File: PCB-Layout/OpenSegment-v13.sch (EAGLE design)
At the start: 45 parts, among them Q1 PNP, Q10 MMBT2222, Q11 MMBT2222, Q12 MMBT2222, Q2 PNP, Q3 PNP, Q4 PNP, Q5 PNP, Q6 PNP, Q7 PNP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

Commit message: Added I2C gang pins, silk color squares, adjusted 10uF cap spot.
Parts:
- removed JP7: Serial, SparkFun-Connectors:M03
- removed SJ3: Counter Ctl, SparkFun-Passives:SOLDERJUMPERNO
- added C1: 0.1uF, SparkFun:CAP0402-CAP
- added JP11: Serial, SparkFun-Connectors:M03JST-PTH
- added JP12, JP13: (no value), SparkFun-Connectors:M02PTH
- added SJ1, SJ2: Counter Ctl, SparkFun-Passives:SOLDERJUMPERNO
- added U$4: OSHW-LOGOS, SparkFun-Aesthetics:OSHW-LOGOS
- JP8: value M01 -> RESET
- R2, R3, R4, R5, R6, R7, R8, R9: value 50 -> 27
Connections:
- net CS renamed !SS
- net MISO renamed SDO
- net MOSI renamed SDI
- removed net N$2: SJ3.1, U2.PB7(XTAL2/TOSC2)
- new net ANALOG: SJ2.1, U2.PB7(XTAL2/TOSC2)
- new net N$11: C1.2, U2.AREF
- net COUNTER: now also SJ1.1; no longer JP2.8
- net GND: now also C1.1, JP11.2, JP12.1, SJ1.2, SJ2.2; no longer JP7.2, SJ3.2
- net RAW: now also JP11.1, JP12.2; no longer JP7.3
- net RXI: now also JP11.3; no longer JP7.1
- net SCL: now also JP13.2
- net SDA: now also JP13.1
- net TXO: now also JP2.8
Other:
- note added: "50 Ohm"
- note added: "Add OSHW logo"
- note added: "Add silk to top side A6/7"
- note added: "Added mode jumpers"
- note added: "Changed SPI pins to SDO/SDI to match"
- note added: "Changes on v1.3:"
- note added: "Close Jumper For:"
- note added: "Decrement"
- note added: "Ganged I2C + pwr"
- note added: "Increment"
- note added: "Measurements show 10mA. Changing to 27 Ohm"
- note added: "Meter Mode"
- note added: "Move in 10uF cap"
- note added: "R = 38.3 Ohm"
- note added: "Silkscreen squares for colors"
- note added: "original S7S"
- note removed: "Changed PB6 to dedicated counter pin"
- note removed: "Removed TXO connection"
- moved on the sheet: C10, C13, C19, C3, C4, JP1, JP10, JP2, JP8, JP9, LED1, R1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

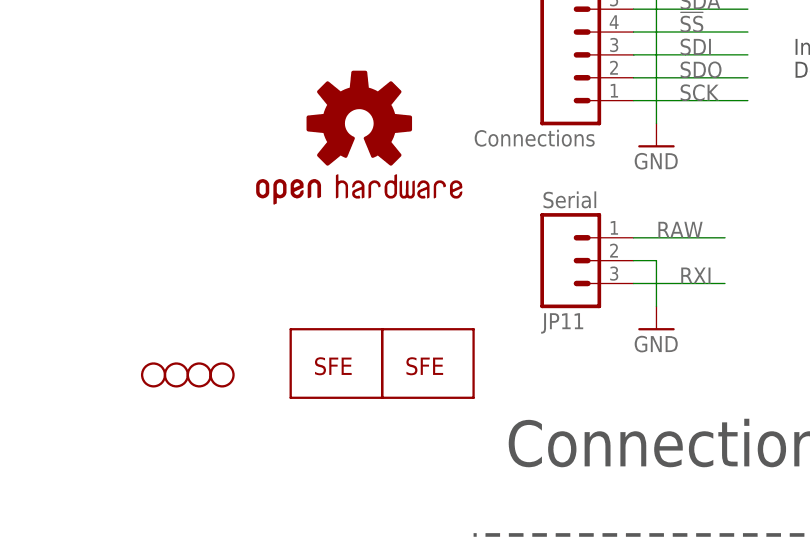
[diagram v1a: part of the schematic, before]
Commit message: Added fiducial markings and created panel
preparing for mass production
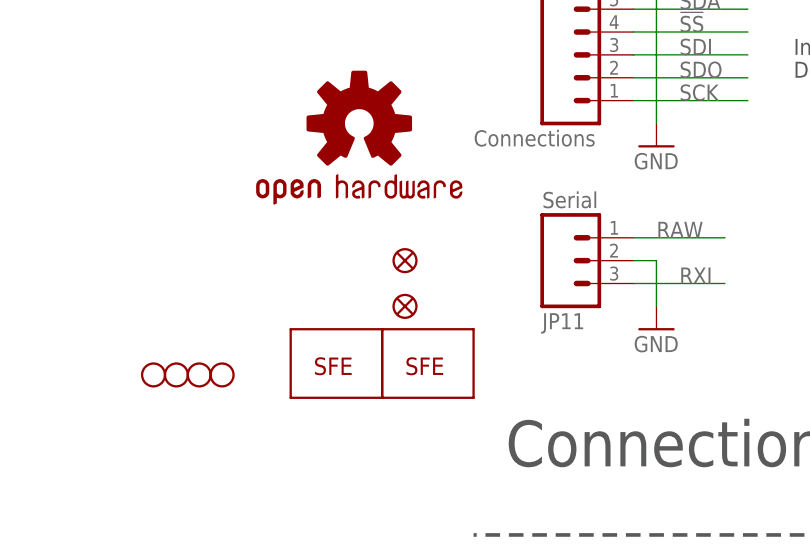
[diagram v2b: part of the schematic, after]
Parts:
- added JP14, JP7: FIDUCIALUFIDUCIAL, SparkFun:FIDUCIALUFIDUCIAL
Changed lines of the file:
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@@
 <part name="JP12" library="SparkFun-Connectors" deviceset="M02" device="PTH"/>
 <part name="JP13" library="SparkFun-Connectors" deviceset="M02" device="PTH"/>
+<part name="JP7" library="SparkFun" deviceset="FIDUCIAL" device="UFIDUCIAL"/>
+<part name="JP14" library="SparkFun" deviceset="FIDUCIAL" device="UFIDUCIAL"/>
 </parts>
 <sheets>
@@
 <instance part="JP12" gate="G$1" x="317.5" y="30.48"/>
 <instance part="JP13" gate="G$1" x="317.5" y="15.24"/>
+<instance part="JP7" gate="G$1" x="241.3" y="30.48"/>
+<instance part="JP14" gate="G$1" x="241.3" y="25.4"/>
 </instances>
 <busses>

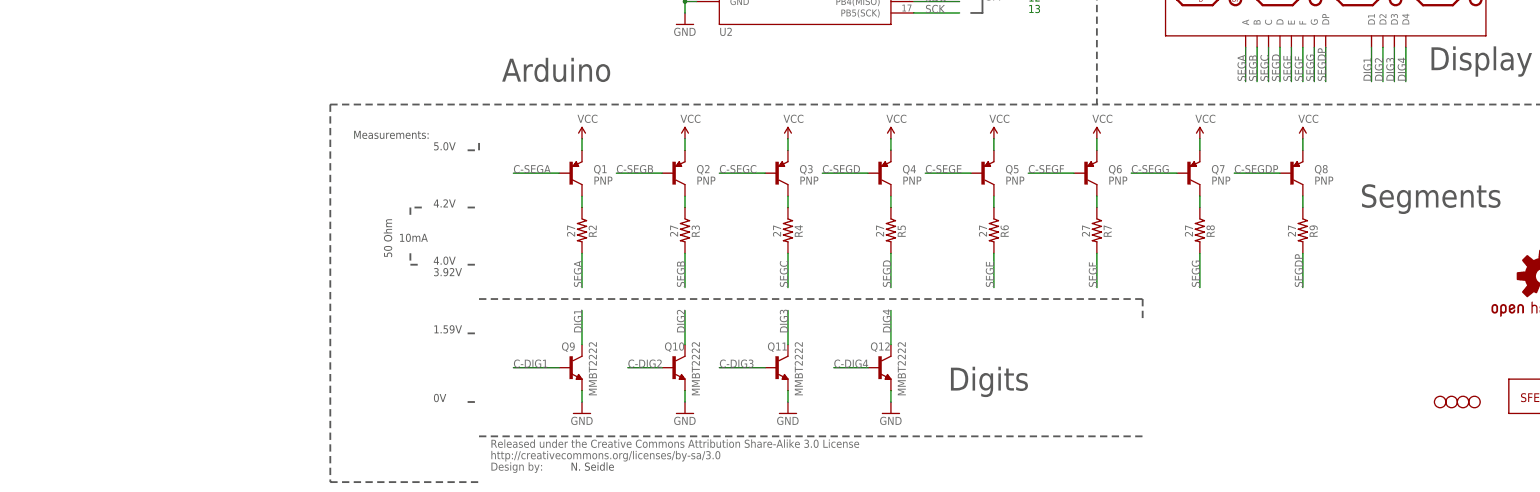
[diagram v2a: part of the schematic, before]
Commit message: Added part #s for transistors and resistor calculations.
The bias resistors on the NPN and PNPs helped. Reducing current through
segments further to hit 10-12mA per segment when on for 25% duty cycle.
Also added calculations for different color displays.
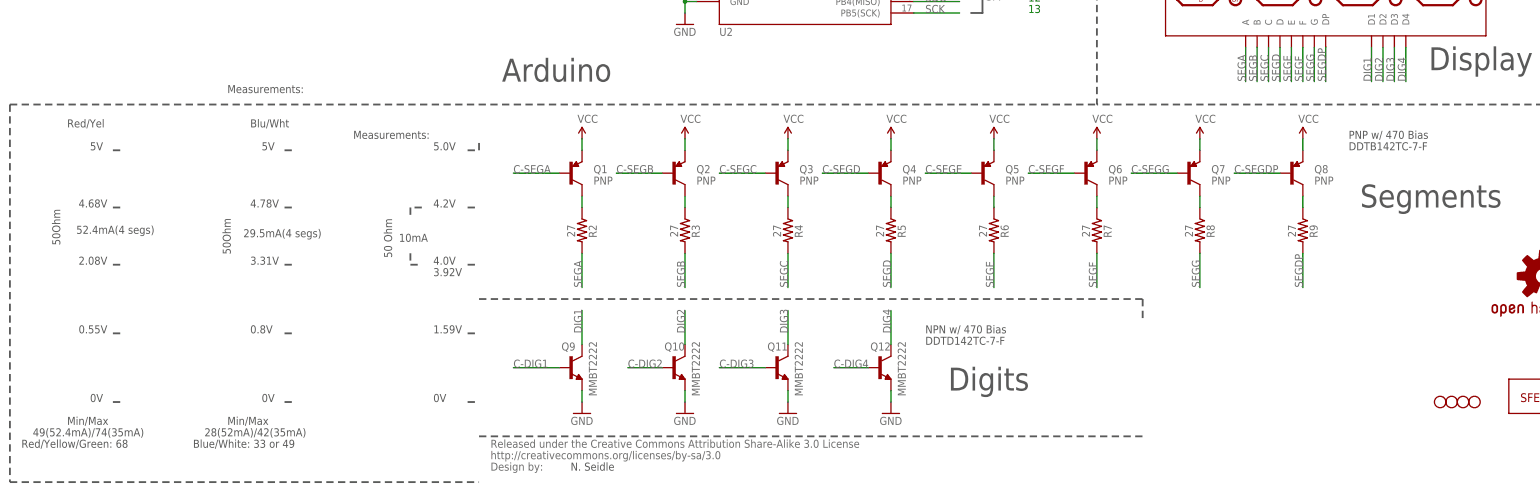
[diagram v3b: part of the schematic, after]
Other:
- note added: "0.55V"
- note added: "0.8V"
- note added: "2.08V"
- note added: "28(52mA)/42(35mA)"
- note added: "29.5mA(4 segs)"
- note added: "3.31V"
- note added: "4.68V"
- note added: "4.78V"
- note added: "49(52.4mA)/74(35mA)"
- note added: "50Ohm"
- note added: "52.4mA(4 segs)"
- note added: "5V"
- note added: "Blu/Wht"
- note added: "Blue/White: 33 or 49"
- note added: "DDTB142TC-7-F"
- note added: "DDTD142TC-7-F"
- note added: "Min/Max"
- note added: "NPN w/ 470 Bias"
- note added: "PNP w/ 470 Bias"
- note added: "Red/Yel"
- note added: "Red/Yellow/Green: 68"
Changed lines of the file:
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@@
 <text x="121.92" y="147.32" size="1.778" layer="91">A6</text>
 <text x="121.92" y="144.78" size="1.778" layer="91">A7</text>
-<wire x1="-33.02" y1="83.82" x2="137.16" y2="83.82" width="0.4064" layer="97" style="shortdash"/>
+<wire x1="-104.14" y1="83.82" x2="137.16" y2="83.82" width="0.4064" layer="97" style="shortdash"/>
 <wire x1="0" y1="40.64" x2="147.32" y2="40.64" width="0.4064" layer="97" style="shortdash"/>
 <wire x1="147.32" y1="40.64" x2="147.32" y2="35.56" width="0.4064" layer="97" style="shortdash"/>
@@
 <text x="284.48" y="50.8" size="1.778" layer="97">Decrement</text>
 <text x="185.42" y="167.64" size="1.778" layer="97">Added mode jumpers</text>
-<wire x1="-33.02" y1="83.82" x2="-33.02" y2="0" width="0.4064" layer="97" style="shortdash"/>
-<wire x1="-33.02" y1="0" x2="0" y2="0" width="0.4064" layer="97" style="shortdash"/>
+<wire x1="-104.14" y1="83.82" x2="-104.14" y2="0" width="0.4064" layer="97" style="shortdash"/>
+<wire x1="-104.14" y1="0" x2="0" y2="0" width="0.4064" layer="97" style="shortdash"/>
 <wire x1="-2.54" y1="60.96" x2="0" y2="60.96" width="0.4064" layer="97" style="shortdash"/>
 <wire x1="-2.54" y1="73.66" x2="0" y2="73.66" width="0.4064" layer="97" style="shortdash"/>
@@
 <text x="185.42" y="149.86" size="1.778" layer="97">Move in 10uF cap</text>
 <text x="182.88" y="154.94" size="1.778" layer="97">Changes on v1.3:</text>
+<text x="-55.88" y="86.36" size="1.778" layer="97">Measurements:</text>
+<text x="-50.8" y="60.96" size="1.778" layer="97">4.78V</text>
+<text x="-50.8" y="48.26" size="1.778" layer="97">3.31V</text>
+<text x="-50.8" y="33.02" size="1.778" layer="97">0.8V</text>
+<text x="-48.26" y="73.66" size="1.778" layer="97">5V</text>
+<text x="-48.26" y="17.78" size="1.778" layer="97">0V</text>
+<text x="-50.8" y="78.74" size="1.778" layer="97">Blu/Wht</text>
+<text x="-91.44" y="78.74" size="1.778" layer="97">Red/Yel</text>
+<text x="-86.36" y="73.66" size="1.778" layer="97">5V</text>
+<text x="-88.9" y="60.96" size="1.778" layer="97">4.68V</text>
+<text x="-88.9" y="48.26" size="1.778" layer="97">2.08V</text>
+<text x="-88.9" y="33.02" size="1.778" layer="97">0.55V</text>
+<text x="-86.36" y="17.78" size="1.778" layer="97">0V</text>
+<text x="-55.118" y="50.546" size="1.778" layer="97" rot="R90">50Ohm</text>
+<text x="-92.964" y="52.578" size="1.778" layer="97" rot="R90">50Ohm</text>
+<text x="-60.96" y="10.16" size="1.778" layer="97">28(52mA)/42(35mA)</text>
+<text x="-99.06" y="10.16" size="1.778" layer="97">49(52.4mA)/74(35mA)</text>
+<text x="-91.44" y="12.7" size="1.778" layer="97">Min/Max</text>
+<text x="-101.6" y="7.62" size="1.778" layer="97">Red/Yellow/Green: 68</text>
+<text x="-63.5" y="7.62" size="1.778" layer="97">Blue/White: 33 or 49</text>
+<text x="-55.88" y="12.7" size="1.778" layer="97">Min/Max</text>
+<wire x1="-43.18" y1="33.02" x2="-40.64" y2="33.02" width="0.4064" layer="97" style="shortdash"/>
+<wire x1="-81.28" y1="33.02" x2="-78.74" y2="33.02" width="0.4064" layer="97" style="shortdash"/>
+<wire x1="-43.18" y1="48.26" x2="-40.64" y2="48.26" width="0.4064" layer="97" style="shortdash"/>
+<wire x1="-43.18" y1="60.96" x2="-40.64" y2="60.96" width="0.4064" layer="97" style="shortdash"/>
+<wire x1="-43.18" y1="73.66" x2="-40.64" y2="73.66" width="0.4064" layer="97" style="shortdash"/>
+<wire x1="-43.18" y1="17.78" x2="-40.64" y2="17.78" width="0.4064" layer="97" style="shortdash"/>
+<wire x1="-81.28" y1="48.26" x2="-78.74" y2="48.26" width="0.4064" layer="97" style="shortdash"/>
+<wire x1="-81.28" y1="60.96" x2="-78.74" y2="60.96" width="0.4064" layer="97" style="shortdash"/>
+<wire x1="-81.28" y1="73.66" x2="-78.74" y2="73.66" width="0.4064" layer="97" style="shortdash"/>
+<wire x1="-81.28" y1="17.78" x2="-78.74" y2="17.78" width="0.4064" layer="97" style="shortdash"/>
+<text x="-89.408" y="55.118" size="1.778" layer="97">52.4mA(4 segs)</text>
+<text x="-52.324" y="54.356" size="1.778" layer="97">29.5mA(4 segs)</text>
+<text x="99.06" y="33.02" size="1.778" layer="97">NPN w/ 470 Bias</text>
+<text x="99.06" y="30.48" size="1.778" layer="97">DDTD142TC-7-F</text>
+<text x="193.04" y="76.2" size="1.778" layer="97">PNP w/ 470 Bias</text>
+<text x="193.04" y="73.66" size="1.778" layer="97">DDTB142TC-7-F</text>
 </plain>
 <instances>

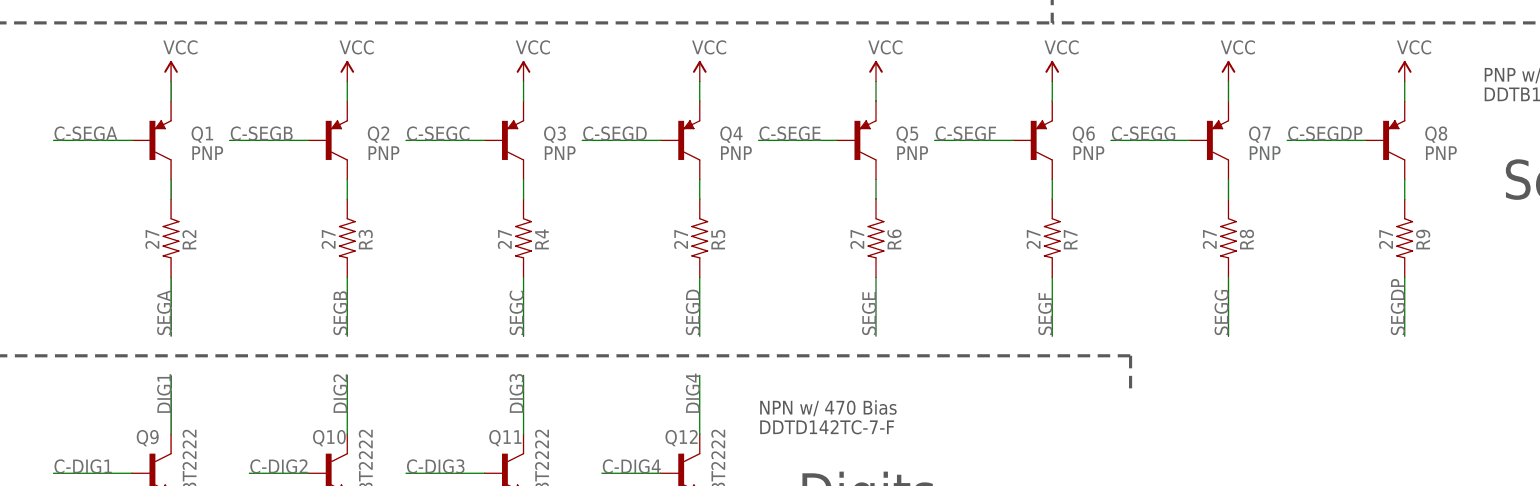
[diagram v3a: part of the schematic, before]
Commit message: Updated resistor values.
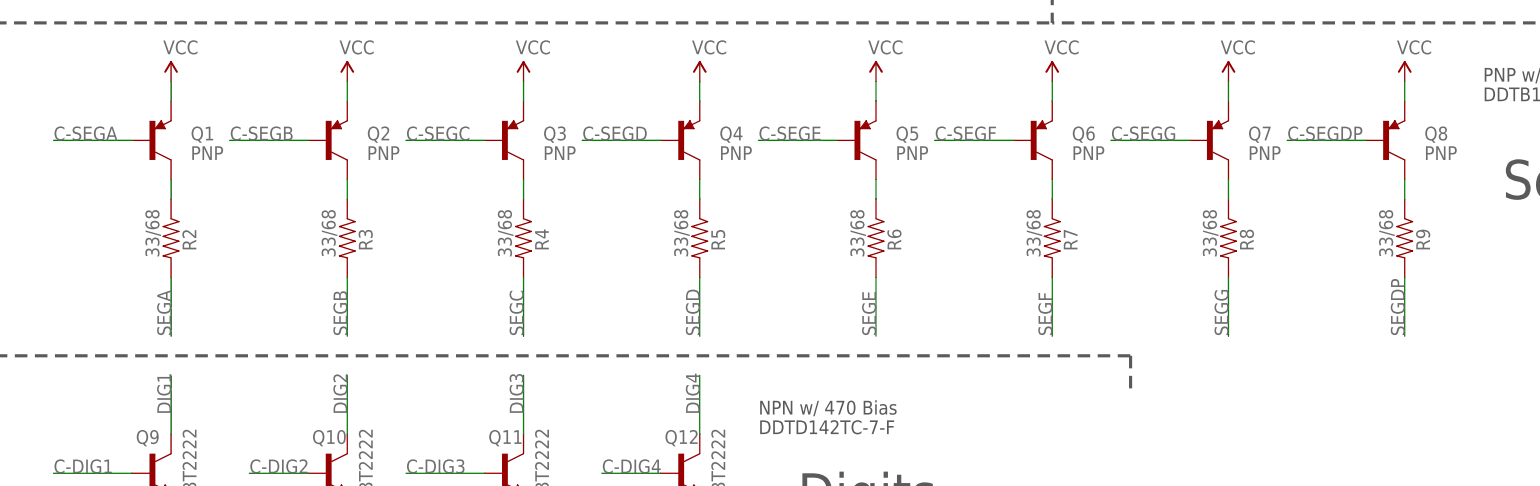
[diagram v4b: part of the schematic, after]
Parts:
- R2, R3, R4, R5, R6, R7, R8, R9: value 27 -> 33/68
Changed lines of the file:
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@@
 <part name="JP5" library="SparkFun-Electromechanical" deviceset="STAND-OFF" device=""/>
 <part name="JP6" library="SparkFun-Electromechanical" deviceset="STAND-OFF" device=""/>
-<part name="R2" library="SparkFun" deviceset="RESISTOR" device="0402-RES" value="27"/>
+<part name="R2" library="SparkFun" deviceset="RESISTOR" device="0402-RES" value="33/68"/>
 <part name="Q1" library="SparkFun-DiscreteSemi" deviceset="TRANSISTOR_PNP" device="SMD" value="PNP"/>
 <part name="SJ2" library="SparkFun-Passives" deviceset="SOLDERJUMPER" device="NO" value="Counter Ctl"/>
@@
 <part name="GND15" library="SparkFun" deviceset="GND" device=""/>
 <part name="JP2" library="SparkFun-Connectors" deviceset="M10" device="&quot;" value="Connections"/>
-<part name="R3" library="SparkFun" deviceset="RESISTOR" device="0402-RES" value="27"/>
-<part name="R4" library="SparkFun" deviceset="RESISTOR" device="0402-RES" value="27"/>
-<part name="R5" library="SparkFun" deviceset="RESISTOR" device="0402-RES" value="27"/>
-<part name="R6" library="SparkFun" deviceset="RESISTOR" device="0402-RES" value="27"/>
-<part name="R7" library="SparkFun" deviceset="RESISTOR" device="0402-RES" value="27"/>
-<part name="R8" library="SparkFun" deviceset="RESISTOR" device="0402-RES" value="27"/>
-<part name="R9" library="SparkFun" deviceset="RESISTOR" device="0402-RES" value="27"/>
+<part name="R3" library="SparkFun" deviceset="RESISTOR" device="0402-RES" value="33/68"/>
+<part name="R4" library="SparkFun" deviceset="RESISTOR" device="0402-RES" value="33/68"/>
+<part name="R5" library="SparkFun" deviceset="RESISTOR" device="0402-RES" value="33/68"/>
+<part name="R6" library="SparkFun" deviceset="RESISTOR" device="0402-RES" value="33/68"/>
+<part name="R7" library="SparkFun" deviceset="RESISTOR" device="0402-RES" value="33/68"/>
+<part name="R8" library="SparkFun" deviceset="RESISTOR" device="0402-RES" value="33/68"/>
+<part name="R9" library="SparkFun" deviceset="RESISTOR" device="0402-RES" value="33/68"/>
 <part name="GND16" library="SparkFun" deviceset="GND" device=""/>
 <part name="U$2" library="SparkFun" deviceset="LOGO-SFE" device="SK"/>
@@
 <instance part="R2" gate="G$1" x="22.86" y="55.88" smashed="yes" rot="R270">
 <attribute name="NAME" x="24.3586" y="57.15" size="1.778" layer="95" rot="R270"/>
-<attribute name="VALUE" x="19.558" y="57.15" size="1.778" layer="96" rot="R270"/>
+<attribute name="VALUE" x="19.558" y="59.69" size="1.778" layer="96" rot="R270"/>
 </instance>
 <instance part="Q1" gate="G$1" x="20.32" y="68.58"/>
@@
 <instance part="R3" gate="G$1" x="45.72" y="55.88" smashed="yes" rot="R270">
 <attribute name="NAME" x="47.2186" y="57.15" size="1.778" layer="95" rot="R270"/>
-<attribute name="VALUE" x="42.418" y="57.15" size="1.778" layer="96" rot="R270"/>
+<attribute name="VALUE" x="42.418" y="59.69" size="1.778" layer="96" rot="R270"/>
 </instance>
 <instance part="R4" gate="G$1" x="68.58" y="55.88" smashed="yes" rot="R270">
 <attribute name="NAME" x="70.0786" y="57.15" size="1.778" layer="95" rot="R270"/>
-<attribute name="VALUE" x="65.278" y="57.15" size="1.778" layer="96" rot="R270"/>
+<attribute name="VALUE" x="65.278" y="59.69" size="1.778" layer="96" rot="R270"/>
 </instance>
 <instance part="R5" gate="G$1" x="91.44" y="55.88" smashed="yes" rot="R270">
 <attribute name="NAME" x="92.9386" y="57.15" size="1.778" layer="95" rot="R270"/>
-<attribute name="VALUE" x="88.138" y="57.15" size="1.778" layer="96" rot="R270"/>
+<attribute name="VALUE" x="88.138" y="59.69" size="1.778" layer="96" rot="R270"/>
 </instance>
 <instance part="R6" gate="G$1" x="114.3" y="55.88" smashed="yes" rot="R270">
 <attribute name="NAME" x="115.7986" y="57.15" size="1.778" layer="95" rot="R270"/>
-<attribute name="VALUE" x="110.998" y="57.15" size="1.778" layer="96" rot="R270"/>
+<attribute name="VALUE" x="110.998" y="59.69" size="1.778" layer="96" rot="R270"/>
 </instance>
 <instance part="R7" gate="G$1" x="137.16" y="55.88" smashed="yes" rot="R270">
 <attribute name="NAME" x="138.6586" y="57.15" size="1.778" layer="95" rot="R270"/>
-<attribute name="VALUE" x="133.858" y="57.15" size="1.778" layer="96" rot="R270"/>
+<attribute name="VALUE" x="133.858" y="59.69" size="1.778" layer="96" rot="R270"/>
 </instance>
 <instance part="R8" gate="G$1" x="160.02" y="55.88" smashed="yes" rot="R270">
 <attribute name="NAME" x="161.5186" y="57.15" size="1.778" layer="95" rot="R270"/>
-<attribute name="VALUE" x="156.718" y="57.15" size="1.778" layer="96" rot="R270"/>
+<attribute name="VALUE" x="156.718" y="59.69" size="1.778" layer="96" rot="R270"/>
 </instance>
 <instance part="R9" gate="G$1" x="182.88" y="55.88" smashed="yes" rot="R270">
 <attribute name="NAME" x="184.3786" y="57.15" size="1.778" layer="95" rot="R270"/>
-<attribute name="VALUE" x="179.578" y="57.15" size="1.778" layer="96" rot="R270"/>
+<attribute name="VALUE" x="179.578" y="59.69" size="1.778" layer="96" rot="R270"/>
 </instance>
 <instance part="GND16" gate="1" x="269.24" y="43.18"/>
